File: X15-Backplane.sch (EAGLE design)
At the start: 37 parts, among them J3 IPL1-103-01-L-S-K, J4 IPL1-104-01-X-S-K

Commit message: Updated
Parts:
- renumbered ESC_CONTROL1 to ESC_CONTROLLER, J3 to ROBOT_CONN, J4 to 7.4V_CONN, PXC-8-RA-1 to SOLENOID, U$9 to DATA_CON_CONN
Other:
- note added: "7.4V Power Input"
- note removed: "7.4V Power to BKP"

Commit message: Hmm
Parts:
- removed PXC-8-RA-1778683: PXC-8-RA-1778683, X15-Backplane Parts:PXC-8-RA-1778683
- R1: value 150,000,000 -> 1500
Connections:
- removed net PROG_1: PXC-8-RA-1778683.7
- removed net PROG_2: PXC-8-RA-1778683.6
- removed net PROG_3: PXC-8-RA-1778683.5
- removed net SWCLK_IN: PXC-8-RA-1778683.2
- removed net SWDIO_IN: PXC-8-RA-1778683.1
- net 3V3: no longer PXC-8-RA-1778683.4
- net GND: no longer PXC-8-RA-1778683.8
- net NRST: no longer PXC-8-RA-1778683.3
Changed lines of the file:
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@@
 <parts>
 <part name="FRAME2" library="SparkFun-Aesthetics" library_urn="urn:adsk.eagle:library:507" deviceset="FRAME-A4L" device=""/>
-<part name="PXC-8-RA-1778683" library="X15-Backplane Parts" deviceset="PXC-8-RA-1778683" device="" package3d_urn="urn:adsk.eagle:package:25224885/2">
-<attribute name="SPICEPREFIX" value="X"/>
-</part>
 <part name="U$4" library="X15-Backplane Parts" deviceset="BACKPLANE_ESC_ADAPTER_PWR" device="BKP"/>
 <part name="U$5" library="X15-Backplane Parts" deviceset="BACKPLANE_ESC_ADAPTER_PWR" device="BKP"/>
@@
 <part name="7.4V_CONN" library="X15-Backplane Parts" deviceset="IPL1-104-01-X-S-K" device=""/>
 <part name="D5" library="SparkFun-LED" library_urn="urn:adsk.eagle:library:529" deviceset="LED" device="3MM" package3d_urn="urn:adsk.eagle:package:39361/1"/>
-<part name="R1" library="SparkFun-Resistors" library_urn="urn:adsk.eagle:library:532" deviceset="RESISTOR" device="0603" package3d_urn="urn:adsk.eagle:package:39650/1" value="150,000,000"/>
 <part name="D7" library="SparkFun-LED" library_urn="urn:adsk.eagle:library:529" deviceset="LED" device="3MM" package3d_urn="urn:adsk.eagle:package:39361/1"/>
 <part name="R3" library="SparkFun-Resistors" library_urn="urn:adsk.eagle:library:532" deviceset="RESISTOR" device="0603" package3d_urn="urn:adsk.eagle:package:39650/1" value="1500"/>
 <part name="D8" library="SparkFun-LED" library_urn="urn:adsk.eagle:library:529" deviceset="LED" device="3MM" package3d_urn="urn:adsk.eagle:package:39361/1"/>
 <part name="R7" library="SparkFun-Resistors" library_urn="urn:adsk.eagle:library:532" deviceset="RESISTOR" device="0603" package3d_urn="urn:adsk.eagle:package:39650/1" value="1500"/>
+<part name="R1" library="SparkFun-Resistors" library_urn="urn:adsk.eagle:library:532" deviceset="RESISTOR" device="0603" package3d_urn="urn:adsk.eagle:package:39650/1" value="1500"/>
 </parts>
 <sheets>
@@
 <attribute name="SHEET" x="200.66" y="8.89" size="2.54" layer="94" font="vector"/>
 </instance>
-<instance part="PXC-8-RA-1778683" gate="G$1" x="38.1" y="119.38" smashed="yes" rot="R180">
-<attribute name="NAME" x="33.02" y="106.68" size="1.778" layer="95"/>
-</instance>
 <instance part="U$4" gate="G$1" x="83.82" y="124.46" smashed="yes">
 <attribute name="NAME" x="81.28" y="121.92" size="1.27" layer="95" rot="R90"/>
@@
 </busses>
 <nets>
-<net name="SWDIO_IN" class="0">
-<segment>
-<pinref part="PXC-8-RA-1778683" gate="G$1" pin="1"/>
-<wire x1="30.48" y1="111.76" x2="17.78" y2="111.76" width="0.1524" layer="91"/>
-<label x="17.78" y="111.76" size="1.778" layer="95"/>
-</segment>
-</net>
 <net name="SWDIO_4" class="0">
 <segment>
@@
 </segment>
 </net>
-<net name="PROG_3" class="0">
-<segment>
-<pinref part="PXC-8-RA-1778683" gate="G$1" pin="5"/>
-<wire x1="30.48" y1="121.92" x2="17.78" y2="121.92" width="0.1524" layer="91"/>
-<label x="20.32" y="121.92" size="1.778" layer="95"/>
-</segment>
-</net>
-<net name="PROG_1" class="0">
-<segment>
-<pinref part="PXC-8-RA-1778683" gate="G$1" pin="7"/>
-<wire x1="30.48" y1="127" x2="17.78" y2="127" width="0.1524" layer="91"/>
-<label x="20.32" y="127" size="1.778" layer="95"/>
-</segment>
-</net>
 <net name="SWCLK_4" class="0">
 <segment>
@@
 </segment>
 </net>
-<net name="SWCLK_IN" class="0">
-<segment>
-<pinref part="PXC-8-RA-1778683" gate="G$1" pin="2"/>
-<wire x1="30.48" y1="114.3" x2="17.78" y2="114.3" width="0.1524" layer="91"/>
-<label x="17.78" y="114.3" size="1.778" layer="95"/>
-</segment>
-</net>
 <net name="3V3" class="0">
-<segment>
-<pinref part="PXC-8-RA-1778683" gate="G$1" pin="4"/>
-<wire x1="30.48" y1="119.38" x2="17.78" y2="119.38" width="0.1524" layer="91"/>
-<label x="20.32" y="119.38" size="1.778" layer="95"/>
-</segment>
 <segment>
 <pinref part="R4" gate="G$1" pin="1"/>
@@
 </net>
 <net name="NRST" class="0">
-<segment>
-<pinref part="PXC-8-RA-1778683" gate="G$1" pin="3"/>
-<wire x1="30.48" y1="116.84" x2="17.78" y2="116.84" width="0.1524" layer="91"/>
-<label x="20.32" y="116.84" size="1.778" layer="95"/>
-</segment>
 <segment>
 <pinref part="D4" gate="G$1" pin="C"/>
@@
 <junction x="170.18" y="137.16"/>
 <label x="185.42" y="137.16" size="1.778" layer="95"/>
-</segment>
-</net>
-<net name="PROG_2" class="0">
-<segment>
-<pinref part="PXC-8-RA-1778683" gate="G$1" pin="6"/>
-<wire x1="30.48" y1="124.46" x2="17.78" y2="124.46" width="0.1524" layer="91"/>
-<label x="20.32" y="124.46" size="1.778" layer="95"/>
 </segment>
 </net>
@@
 </segment>
 <segment>
-<pinref part="PXC-8-RA-1778683" gate="G$1" pin="8"/>
-<wire x1="30.48" y1="129.54" x2="17.78" y2="129.54" width="0.1524" layer="91"/>
-<label x="20.32" y="129.54" size="1.778" layer="95"/>
-</segment>
-<segment>
 <pinref part="DATA_CON_CONN" gate="G$1" pin="2"/>
 <wire x1="160.02" y1="86.36" x2="172.72" y2="86.36" width="0.1524" layer="91"/>
@@
 <attribute name="VALUE" x="192.405" y="112.268" size="1.778" layer="96" font="vector" rot="R90" align="top-left"/>
 </instance>
+<instance part="D7" gate="G$1" x="193.04" y="68.58" smashed="yes">
+<attribute name="NAME" x="189.611" y="64.008" size="1.778" layer="95" font="vector" rot="R90"/>
+<attribute name="VALUE" x="194.945" y="64.008" size="1.778" layer="96" font="vector" rot="R90" align="top-left"/>
+</instance>
+<instance part="R3" gate="G$1" x="193.04" y="55.88" smashed="yes" rot="R270">
+<attribute name="NAME" x="194.564" y="55.88" size="1.778" layer="95" font="vector" rot="R270" align="bottom-center"/>
+<attribute name="VALUE" x="191.516" y="55.88" size="1.778" layer="96" font="vector" rot="R270" align="top-center"/>
+</instance>
+<instance part="D8" gate="G$1" x="233.68" y="68.58" smashed="yes">
+<attribute name="NAME" x="230.251" y="64.008" size="1.778" layer="95" font="vector" rot="R90"/>
+<attribute name="VALUE" x="235.585" y="64.008" size="1.778" layer="96" font="vector" rot="R90" align="top-left"/>
+</instance>
+<instance part="R7" gate="G$1" x="233.68" y="55.88" smashed="yes" rot="R270">
+<attribute name="NAME" x="235.204" y="55.88" size="1.778" layer="95" font="vector" rot="R270" align="bottom-center"/>
+<attribute name="VALUE" x="232.156" y="55.88" size="1.778" layer="96" font="vector" rot="R270" align="top-center"/>
+</instance>
 <instance part="R1" gate="G$1" x="190.5" y="104.14" smashed="yes" rot="R270">
 <attribute name="NAME" x="192.024" y="104.14" size="1.778" layer="95" font="vector" rot="R270" align="bottom-center"/>
 <attribute name="VALUE" x="188.976" y="104.14" size="1.778" layer="96" font="vector" rot="R270" align="top-center"/>
-</instance>
-<instance part="D7" gate="G$1" x="193.04" y="68.58" smashed="yes">
-<attribute name="NAME" x="189.611" y="64.008" size="1.778" layer="95" font="vector" rot="R90"/>
-<attribute name="VALUE" x="194.945" y="64.008" size="1.778" layer="96" font="vector" rot="R90" align="top-left"/>
-</instance>
-<instance part="R3" gate="G$1" x="193.04" y="55.88" smashed="yes" rot="R270">
-<attribute name="NAME" x="194.564" y="55.88" size="1.778" layer="95" font="vector" rot="R270" align="bottom-center"/>
-<attribute name="VALUE" x="191.516" y="55.88" size="1.778" layer="96" font="vector" rot="R270" align="top-center"/>
-</instance>
-<instance part="D8" gate="G$1" x="233.68" y="68.58" smashed="yes">
-<attribute name="NAME" x="230.251" y="64.008" size="1.778" layer="95" font="vector" rot="R90"/>
-<attribute name="VALUE" x="235.585" y="64.008" size="1.778" layer="96" font="vector" rot="R90" align="top-left"/>
-</instance>
-<instance part="R7" gate="G$1" x="233.68" y="55.88" smashed="yes" rot="R270">
-<attribute name="NAME" x="235.204" y="55.88" size="1.778" layer="95" font="vector" rot="R270" align="bottom-center"/>
-<attribute name="VALUE" x="232.156" y="55.88" size="1.778" layer="96" font="vector" rot="R270" align="top-center"/>
 </instance>
 </instances>
@@
 </segment>
 <segment>
-<pinref part="R1" gate="G$1" pin="2"/>
 <wire x1="190.5" y1="99.06" x2="190.5" y2="93.98" width="0.1524" layer="91"/>
 <wire x1="190.5" y1="93.98" x2="198.12" y2="93.98" width="0.1524" layer="91"/>
 <label x="198.12" y="93.98" size="1.778" layer="95"/>
+<pinref part="R1" gate="G$1" pin="2"/>
 </segment>
 <segment>
@@
 <segment>
 <pinref part="D5" gate="G$1" pin="C"/>
+<wire x1="190.5" y1="111.76" x2="190.5" y2="109.22" width="0.1524" layer="91"/>
 <pinref part="R1" gate="G$1" pin="1"/>
-<wire x1="190.5" y1="111.76" x2="190.5" y2="109.22" width="0.1524" layer="91"/>
-</segment>
-</net>
+</segment>
+</net>

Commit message: update
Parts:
- removed D4: 0.5A/40V/420mV, SparkFun-DiscreteSemi:DIODE-SCHOTTKY-PMEG4005EJ
- removed R4: 10k, SparkFun-Resistors:RESISTOR0603
- removed U$7: (no value), X15-Backplane Parts:DISCRETECOMPONENTS_SWITCH
- added U1: ULN2003AD, X15-Pi-Shield-Parts:ULN2003AD
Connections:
- new net GPIO1: PI_SHIELD_CONN1.14, U1.IN1
- new net GPIO2: PI_SHIELD_CONN1.16, U1.IN2
- new net GPIO3: PI_SHIELD_CONN1.18, U1.IN3
- new net GPIO4: PI_SHIELD_CONN1.20, U1.IN4
- new net GPIO5: PI_SHIELD_CONN1.22, U1.IN5
- new net GPIO6: PI_SHIELD_CONN1.24, U1.IN6
- new net ROBOT_ARM_2: PI_SHIELD_CONN1.3
- net 12V: now also U1.COM
- net 3V3: no longer R4.1
- net GND: now also U1.GND; no longer U$7.P$1
- net NRST: no longer D4.C, R4.2, U$7.P$2
- net NRST_4: no longer D4.A
- net SOL1_1: now also U1.OUT1; no longer PI_SHIELD_CONN1.14
- net SOL2_1: now also U1.OUT2; no longer PI_SHIELD_CONN1.16
- net SOL3_1: now also U1.OUT3; no longer PI_SHIELD_CONN1.18
- net SOL4_1: now also U1.OUT4; no longer PI_SHIELD_CONN1.20
- net SOL5_1: now also U1.OUT5; no longer PI_SHIELD_CONN1.22
- net SOL6_1: now also U1.OUT6; no longer PI_SHIELD_CONN1.24

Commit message: Hmm
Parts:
- D5, D6, D7, D8: device SparkFun-LED:LED3MM -> SparkFun-LED:LED0603
- R1: value 1500 -> 600
- R2: value 1500 -> 370
- R3: value 1500 -> 150
- R7: value 1500 -> 250
- ROBOT_CONN: value IPL1-103-01-L-S-K -> IPL1-104-01-X-S-K; device X15-Backplane Parts:IPL1-103-01-L-S-K -> X15-Backplane Parts:IPL1-104-01-X-S-K
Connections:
- net 12V: no longer U1.COM
- net 12V_L: now also U1.COM; no longer PI_SHIELD_CONN1.13, PI_SHIELD_CONN1.15
- net ROBOT_ARM_2: now also ROBOT_CONN.04
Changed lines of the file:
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@@
 <part name="C12" library="X15-Backplane Parts" deviceset="UCM1H331MNL1GS" device="" package3d_urn="urn:adsk.eagle:package:24202090/2" value="330uF"/>
 <part name="ESC_CONTROLLER" library="X15-Backplane Parts" deviceset="BACKPLANE_CONNECTORS" device="BKP"/>
-<part name="D6" library="SparkFun-LED" library_urn="urn:adsk.eagle:library:529" deviceset="LED" device="3MM" package3d_urn="urn:adsk.eagle:package:39361/1"/>
-<part name="R2" library="SparkFun-Resistors" library_urn="urn:adsk.eagle:library:532" deviceset="RESISTOR" device="0603" package3d_urn="urn:adsk.eagle:package:39650/1" value="1500"/>
+<part name="D6" library="SparkFun-LED" library_urn="urn:adsk.eagle:library:529" deviceset="LED" device="0603" package3d_urn="urn:adsk.eagle:package:39354/1"/>
+<part name="R2" library="SparkFun-Resistors" library_urn="urn:adsk.eagle:library:532" deviceset="RESISTOR" device="0603" package3d_urn="urn:adsk.eagle:package:39650/1" value="370"/>
 <part name="PI_SHIELD_CONN1" library="X15-Backplane Parts" deviceset="8X_CONN" device=""/>
-<part name="ROBOT_CONN" library="X15-Backplane Parts" deviceset="IPL1-103-01-L-S-K" device=""/>
+<part name="ROBOT_CONN" library="X15-Backplane Parts" deviceset="IPL1-104-01-X-S-K" device=""/>
 <part name="7.4V_CONN" library="X15-Backplane Parts" deviceset="IPL1-104-01-X-S-K" device=""/>
-<part name="D5" library="SparkFun-LED" library_urn="urn:adsk.eagle:library:529" deviceset="LED" device="3MM" package3d_urn="urn:adsk.eagle:package:39361/1"/>
-<part name="D7" library="SparkFun-LED" library_urn="urn:adsk.eagle:library:529" deviceset="LED" device="3MM" package3d_urn="urn:adsk.eagle:package:39361/1"/>
-<part name="R3" library="SparkFun-Resistors" library_urn="urn:adsk.eagle:library:532" deviceset="RESISTOR" device="0603" package3d_urn="urn:adsk.eagle:package:39650/1" value="1500"/>
-<part name="D8" library="SparkFun-LED" library_urn="urn:adsk.eagle:library:529" deviceset="LED" device="3MM" package3d_urn="urn:adsk.eagle:package:39361/1"/>
-<part name="R7" library="SparkFun-Resistors" library_urn="urn:adsk.eagle:library:532" deviceset="RESISTOR" device="0603" package3d_urn="urn:adsk.eagle:package:39650/1" value="1500"/>
-<part name="R1" library="SparkFun-Resistors" library_urn="urn:adsk.eagle:library:532" deviceset="RESISTOR" device="0603" package3d_urn="urn:adsk.eagle:package:39650/1" value="1500"/>
+<part name="D5" library="SparkFun-LED" library_urn="urn:adsk.eagle:library:529" deviceset="LED" device="0603" package3d_urn="urn:adsk.eagle:package:39354/1"/>
+<part name="D7" library="SparkFun-LED" library_urn="urn:adsk.eagle:library:529" deviceset="LED" device="0603" package3d_urn="urn:adsk.eagle:package:39354/1"/>
+<part name="R3" library="SparkFun-Resistors" library_urn="urn:adsk.eagle:library:532" deviceset="RESISTOR" device="0603" package3d_urn="urn:adsk.eagle:package:39650/1" value="150"/>
+<part name="D8" library="SparkFun-LED" library_urn="urn:adsk.eagle:library:529" deviceset="LED" device="0603" package3d_urn="urn:adsk.eagle:package:39354/1"/>
+<part name="R7" library="SparkFun-Resistors" library_urn="urn:adsk.eagle:library:532" deviceset="RESISTOR" device="0603" package3d_urn="urn:adsk.eagle:package:39650/1" value="250"/>
+<part name="R1" library="SparkFun-Resistors" library_urn="urn:adsk.eagle:library:532" deviceset="RESISTOR" device="0603" package3d_urn="urn:adsk.eagle:package:39650/1" value="600"/>
 <part name="U1" library="X15-Pi-Shield-Parts" deviceset="ULN2003AD" device=""/>
 </parts>
@@
 <attribute name="NAME" x="53.975" y="55.245" size="1.778" layer="95" font="vector"/>
 </instance>
-<instance part="ROBOT_CONN" gate="G$1" x="50.8" y="142.24" smashed="yes">
-<attribute name="NAME" x="45.72" y="148.59" size="1.778" layer="95"/>
-<attribute name="VALUE" x="45.72" y="134.62" size="1.778" layer="96"/>
+<instance part="ROBOT_CONN" gate="G$1" x="58.42" y="139.7" smashed="yes">
+<attribute name="NAME" x="53.34" y="148.59" size="1.778" layer="95"/>
+<attribute name="VALUE" x="53.34" y="132.08" size="1.778" layer="96"/>
 </instance>
 <instance part="7.4V_CONN" gate="G$1" x="45.72" y="104.14" smashed="yes">
@@
 <wire x1="190.5" y1="124.46" x2="198.12" y2="124.46" width="0.1524" layer="91"/>
 <label x="198.12" y="124.46" size="1.778" layer="95"/>
-</segment>
-<segment>
-<pinref part="U1" gate="G$1" pin="COM"/>
-<wire x1="134.62" y1="101.6" x2="134.62" y2="114.3" width="0.1524" layer="91"/>
-<label x="134.62" y="111.76" size="1.778" layer="95" rot="R90" align="bottom-right"/>
 </segment>
 </net>
@@
 <segment>
 <pinref part="ROBOT_CONN" gate="G$1" pin="01"/>
-<wire x1="40.64" y1="144.78" x2="27.94" y2="144.78" width="0.1524" layer="91"/>
+<wire x1="48.26" y1="144.78" x2="27.94" y2="144.78" width="0.1524" layer="91"/>
 <label x="30.48" y="144.78" size="1.778" layer="95"/>
 </segment>
@@
 <segment>
 <pinref part="ROBOT_CONN" gate="G$1" pin="02"/>
-<wire x1="40.64" y1="142.24" x2="27.94" y2="142.24" width="0.1524" layer="91"/>
+<wire x1="48.26" y1="142.24" x2="27.94" y2="142.24" width="0.1524" layer="91"/>
 <label x="30.48" y="142.24" size="1.778" layer="95"/>
 </segment>
@@
 <segment>
 <pinref part="ROBOT_CONN" gate="G$1" pin="03"/>
-<wire x1="40.64" y1="139.7" x2="27.94" y2="139.7" width="0.1524" layer="91"/>
+<wire x1="48.26" y1="139.7" x2="27.94" y2="139.7" width="0.1524" layer="91"/>
 <label x="30.48" y="139.7" size="1.778" layer="95"/>
 </segment>
@@
 <net name="12V_L" class="0">
 <segment>
-<pinref part="PI_SHIELD_CONN1" gate="G$1" pin="13"/>
-<wire x1="50.8" y1="52.07" x2="40.64" y2="52.07" width="0.1524" layer="91"/>
-<label x="43.18" y="52.07" size="1.778" layer="95"/>
-</segment>
-<segment>
-<pinref part="PI_SHIELD_CONN1" gate="G$1" pin="15"/>
-<wire x1="50.8" y1="49.53" x2="40.64" y2="49.53" width="0.1524" layer="91"/>
-<label x="43.18" y="49.53" size="1.778" layer="95"/>
+<pinref part="U1" gate="G$1" pin="COM"/>
+<wire x1="134.62" y1="101.6" x2="134.62" y2="114.3" width="0.1524" layer="91"/>
+<label x="134.62" y="111.76" size="1.778" layer="95" rot="R90" align="bottom-right"/>
 </segment>
 </net>
@@
 <label x="30.48" y="33.02" size="1.778" layer="95"/>
 </segment>
-</net>
+<segment>
+<pinref part="ROBOT_CONN" gate="G$1" pin="04"/>
+<wire x1="48.26" y1="137.16" x2="27.94" y2="137.16" width="0.1524" layer="91"/>
+<label x="30.48" y="137.16" size="1.778" layer="95"/>
+</segment>
+</net>

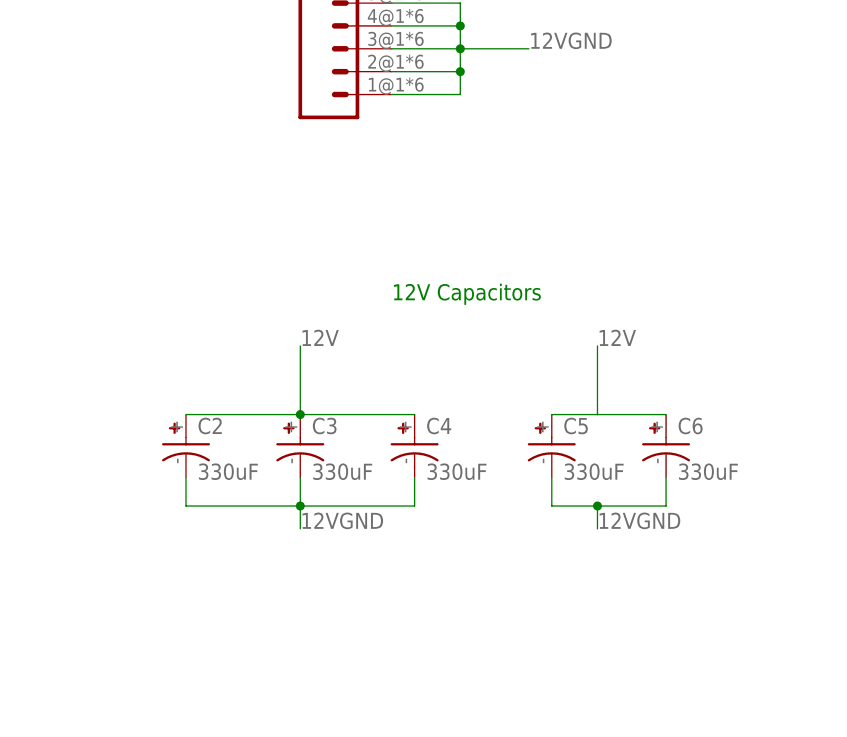
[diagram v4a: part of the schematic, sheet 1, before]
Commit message: Capacitor Changed
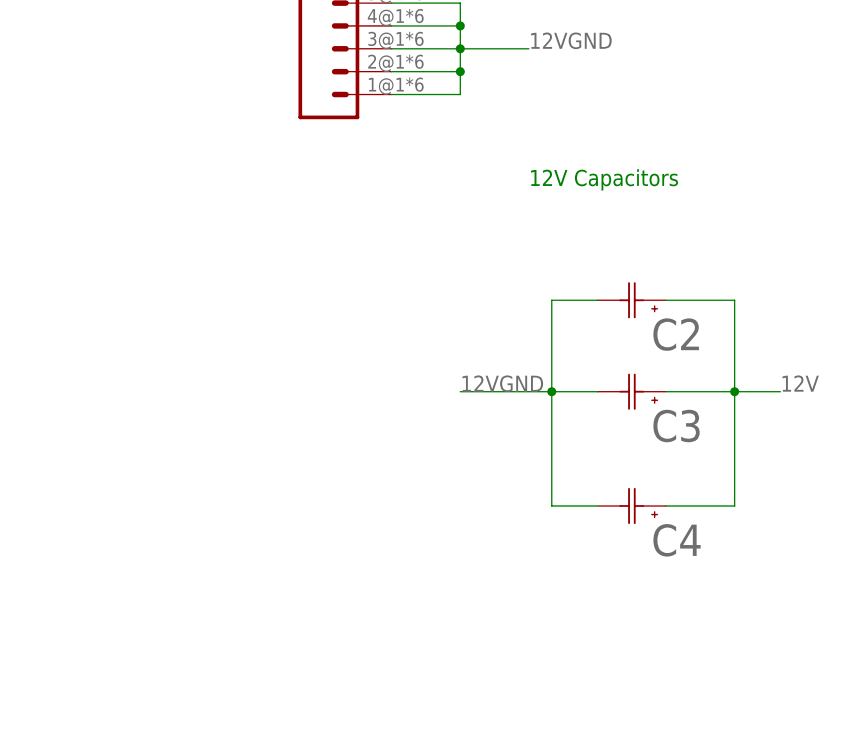
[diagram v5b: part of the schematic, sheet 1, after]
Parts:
- removed C10, C11, C12: 330uF, X15-Backplane Parts:UCM1H331MNL1GS
- C2, C3, C4, C5, C6: value 330uF -> UCV1E561MNL1GSCAP_UCD_8X10_NCH; device X15-Backplane Parts:UCM1H331MNL1GS -> 2023-01-03_19-29-37_Library:UCV1E561MNL1GSCAP_UCD_8X10_NCH
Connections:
- net 12V: now also C2.1, C3.1, C4.1; no longer C2.+, C3.+, C4.+, C5.+, C6.+
- net 12VGND: now also C2.2, C3.2, C4.2; no longer C2.-, C3.-, C4.-, C5.-, C6.-
- net 7.4V: now also C5.1, C6.1; no longer C10.+, C11.+, C12.+
- net 7.4VGND: now also C5.2, C6.2; no longer C10.-, C11.-, C12.-
